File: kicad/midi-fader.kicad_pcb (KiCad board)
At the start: 2 copper layers, 73.7 x 78.7 mm, 163 parts, among them J1 SWD, J2 EXTERNAL_OUT, J3 EXTERNAL_IN, J4 USB_OTG, SW1 TR2-21-L5, SW2 TR2-21-L5, U1 STM32F042KxT, U2 USBLC6-2, U3 MCP1603, U4 MIC2776L, U5 MIC5501-XYM5, U6 74HC165, U7 STP08DP05

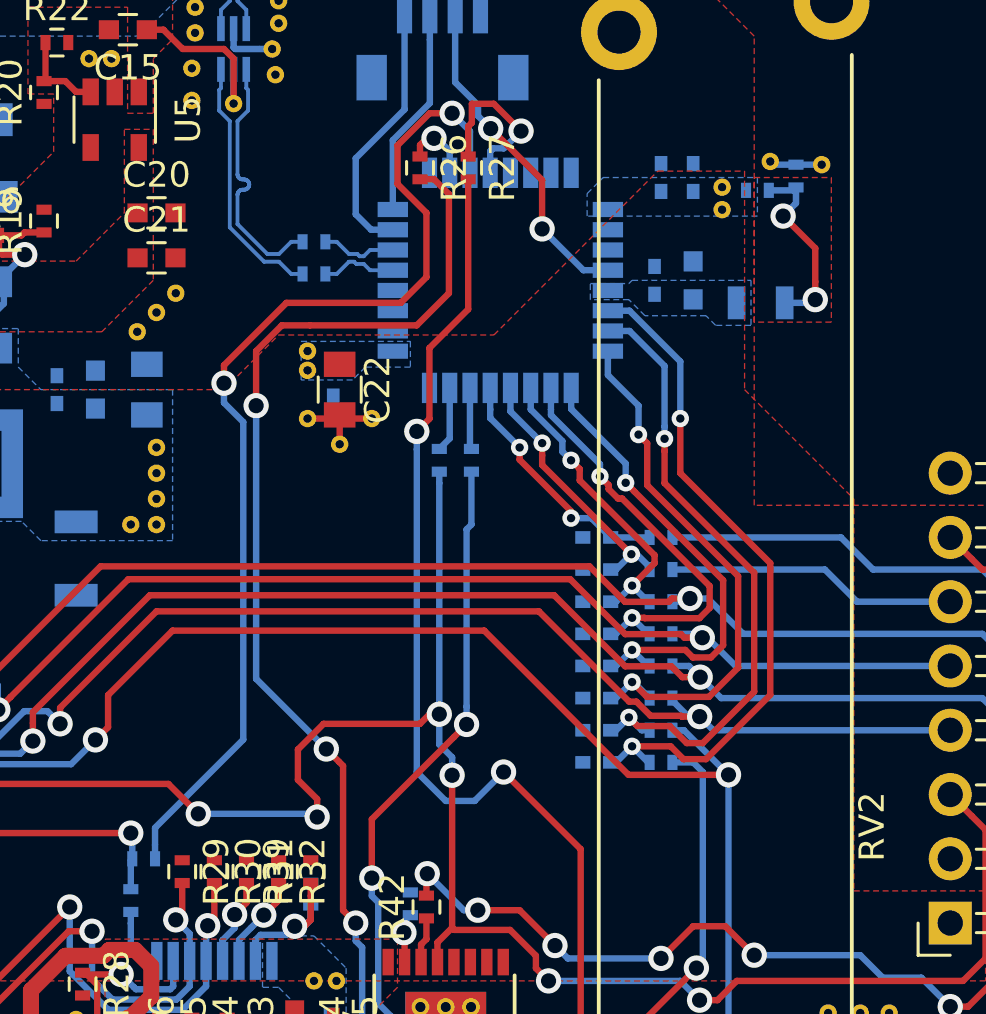
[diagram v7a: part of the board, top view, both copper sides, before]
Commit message: Marked no-connects and changed some plane shapes
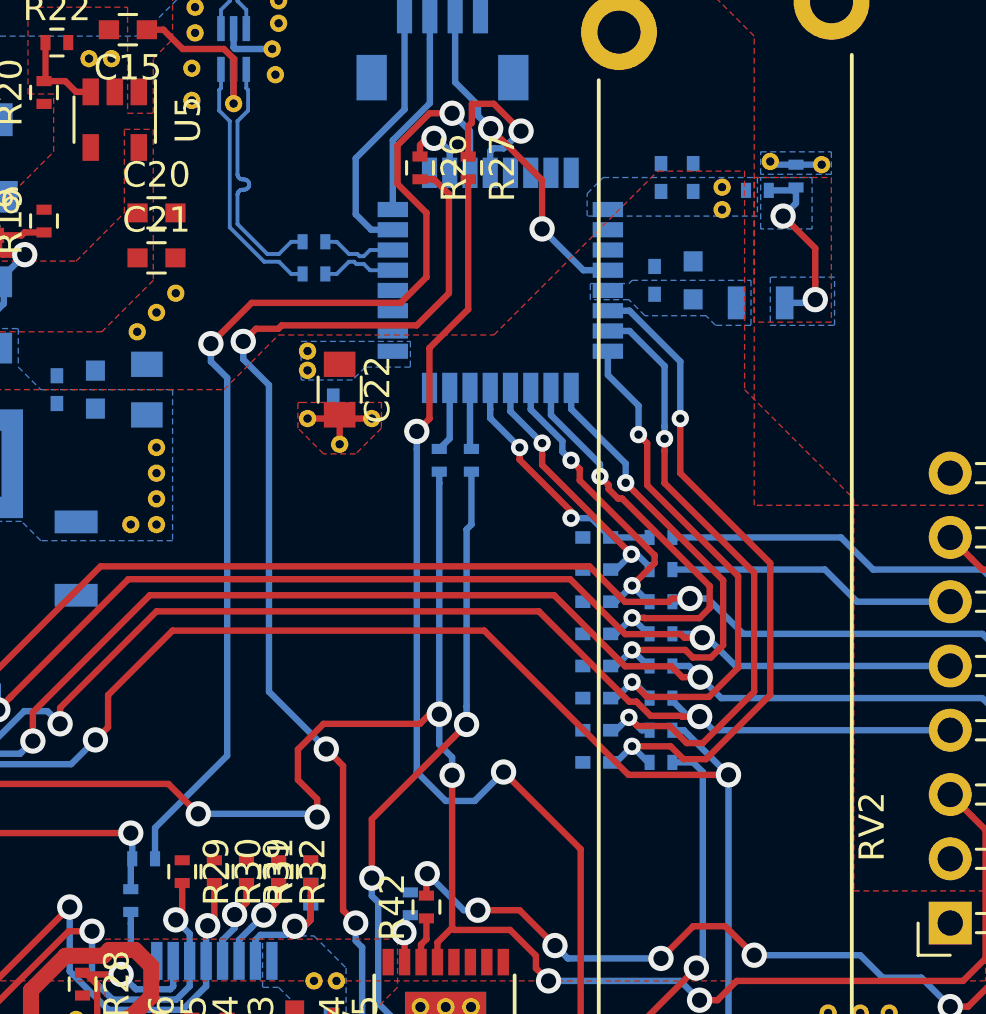
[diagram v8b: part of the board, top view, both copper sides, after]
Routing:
- net /Digital Control/SCLK: track 126.4 -> 127.3 mm
- net /Digital Control/MISO: track 41.7 -> 42.4 mm
- added copper zone on B.Cu, net /Digital Control/VDDA_UC_PREFILT
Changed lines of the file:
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@@
     (thickness 1.6)
     (drawings 9)
-    (tracks 961)
+    (tracks 960)
     (zones 0)
     (modules 163)
@@
     (pad_to_mask_clearance 0.1524)
     (aux_axis_origin 0 0)
+    (grid_origin 117.221 141.859)
     (visible_elements FFFFFF7F)
     (pcbplotparams
@@
   (segment (start 154.94 105.609106) (end 155.194 105.863106) (width 0.254) (layer B.Cu) (net 56))
   (via (at 154.94 104.902) (size 1) (drill 0.6) (layers F.Cu B.Cu) (net 56))
+  (segment (start 149.86 83.693) (end 150.359999 83.193001) (width 0.254) (layer F.Cu) (net 57))
+  (segment (start 157.988 81.788) (end 157.988 77.874) (width 0.254) (layer F.Cu) (net 57))
+  (segment (start 157.988 77.874) (end 157.399 77.285) (width 0.254) (layer F.Cu) (net 57))
+  (segment (start 150.359999 83.193001) (end 151.248999 83.193001) (width 0.254) (layer F.Cu) (net 57))
+  (segment (start 151.248999 83.193001) (end 151.384 83.058) (width 0.254) (layer F.Cu) (net 57))
+  (segment (start 151.384 83.058) (end 156.718 83.058) (width 0.254) (layer F.Cu) (net 57))
+  (segment (start 156.718 83.058) (end 157.988 81.788) (width 0.254) (layer F.Cu) (net 57))
+  (segment (start 157.399 77.285) (end 156.845 77.285) (width 0.254) (layer F.Cu) (net 57))
+  (segment (start 153.141627 99.801627) (end 150.876 97.536) (width 0.254) (layer B.Cu) (net 57))
+  (segment (start 150.876 97.536) (end 150.876 85.416106) (width 0.254) (layer B.Cu) (net 57))
+  (segment (start 150.876 85.416106) (end 149.86 84.400106) (width 0.254) (layer B.Cu) (net 57))
+  (segment (start 149.86 84.400106) (end 149.86 83.693) (width 0.254) (layer B.Cu) (net 57))
+  (via (at 149.86 83.693) (size 1) (drill 0.6) (layers F.Cu B.Cu) (net 57))
   (segment (start 177.673 114.427) (end 170.942 121.158) (width 0.254) (layer B.Cu) (net 57))
   (segment (start 170.942 121.158) (end 159.512 121.158) (width 0.254) (layer B.Cu) (net 57))
@@
   (via (at 156.972 116.713) (size 1) (drill 0.6) (layers F.Cu B.Cu) (net 57))
   (segment (start 156.886 113.773) (end 156.886 116.627) (width 0.254) (layer F.Cu) (net 57))
-  (segment (start 152.641628 99.301628) (end 153.141627 99.801627) (width 0.254) (layer B.Cu) (net 57))
-  (segment (start 150.368 97.028) (end 152.641628 99.301628) (width 0.254) (layer B.Cu) (net 57))
-  (segment (start 150.368 86.233) (end 150.368 97.028) (width 0.254) (layer B.Cu) (net 57))
   (segment (start 153.641626 100.301626) (end 153.141627 99.801627) (width 0.254) (layer F.Cu) (net 57))
   (segment (start 153.805001 100.465001) (end 153.641626 100.301626) (width 0.254) (layer F.Cu) (net 57))
@@
   (segment (start 154.305 107.387106) (end 154.559 107.641106) (width 0.254) (layer B.Cu) (net 57))
   (via (at 154.305 106.68) (size 1) (drill 0.6) (layers F.Cu B.Cu) (net 57))
-  (segment (start 151.384 83.058) (end 150.368 84.074) (width 0.254) (layer F.Cu) (net 57))
-  (segment (start 150.368 84.074) (end 150.368 86.233) (width 0.254) (layer F.Cu) (net 57))
-  (via (at 150.368 86.233) (size 1) (drill 0.6) (layers F.Cu B.Cu) (net 57))
-  (segment (start 152.494994 83.058) (end 151.384 83.058) (width 0.254) (layer F.Cu) (net 57))
-  (segment (start 156.718 83.058) (end 152.494994 83.058) (width 0.254) (layer F.Cu) (net 57))
-  (segment (start 157.988 81.788) (end 156.718 83.058) (width 0.254) (layer F.Cu) (net 57))
-  (segment (start 157.988 77.874) (end 157.988 81.788) (width 0.254) (layer F.Cu) (net 57))
-  (segment (start 156.845 77.285) (end 157.399 77.285) (width 0.254) (layer F.Cu) (net 57))
-  (segment (start 157.399 77.285) (end 157.988 77.874) (width 0.254) (layer F.Cu) (net 57))
   (segment (start 158.82 85.53) (end 158.82 87.885) (width 0.254) (layer B.Cu) (net 58))
   (segment (start 158.82 87.885) (end 158.877 87.942) (width 0.254) (layer B.Cu) (net 58))
@@
   (segment (start 145.288 112.903) (end 145.288 111.829) (width 0.254) (layer F.Cu) (net 70))
   (via (at 145.288 112.903) (size 1) (drill 0.6) (layers F.Cu B.Cu) (net 70))
-  (segment (start 146.373 103.586) (end 146.373 104.14) (width 0.254) (layer B.Cu) (net 71))
-  (segment (start 146.373 102.917486) (end 146.373 103.586) (width 0.254) (layer B.Cu) (net 71))
-  (segment (start 149.86 86.878514) (end 149.86 99.430486) (width 0.254) (layer B.Cu) (net 71))
-  (segment (start 149.098 85.344) (end 149.098 86.116514) (width 0.254) (layer B.Cu) (net 71))
-  (segment (start 149.86 99.430486) (end 146.373 102.917486) (width 0.254) (layer B.Cu) (net 71))
-  (segment (start 149.098 86.116514) (end 149.86 86.878514) (width 0.254) (layer B.Cu) (net 71))
-  (segment (start 149.098 84.636894) (end 149.098 85.344) (width 0.254) (layer F.Cu) (net 71))
-  (segment (start 156.083 82.169) (end 151.565894 82.169) (width 0.254) (layer F.Cu) (net 71))
-  (segment (start 157.099 81.153) (end 156.083 82.169) (width 0.254) (layer F.Cu) (net 71))
-  (segment (start 151.565894 82.169) (end 149.098 84.636894) (width 0.254) (layer F.Cu) (net 71))
-  (segment (start 157.099 78.613) (end 157.099 81.153) (width 0.254) (layer F.Cu) (net 71))
-  (segment (start 155.956 77.47) (end 157.099 78.613) (width 0.254) (layer F.Cu) (net 71))
-  (segment (start 155.956 75.946) (end 155.956 77.47) (width 0.254) (layer F.Cu) (net 71))
-  (segment (start 157.226 74.676) (end 155.956 75.946) (width 0.254) (layer F.Cu) (net 71))
   (segment (start 158.115 74.676) (end 157.226 74.676) (width 0.254) (layer F.Cu) (net 71))
-  (via (at 149.098 85.344) (size 1) (drill 0.6) (layers F.Cu B.Cu) (net 71))
+  (segment (start 157.226 74.676) (end 155.956 75.946) (width 0.254) (layer F.Cu) (net 71))
+  (segment (start 155.956 75.946) (end 155.956 77.47) (width 0.254) (layer F.Cu) (net 71))
+  (segment (start 155.956 77.47) (end 157.099 78.613) (width 0.254) (layer F.Cu) (net 71))
+  (segment (start 157.099 78.613) (end 157.099 81.153) (width 0.254) (layer F.Cu) (net 71))
+  (segment (start 157.099 81.153) (end 156.083 82.169) (width 0.254) (layer F.Cu) (net 71))
+  (segment (start 156.083 82.169) (end 150.193293 82.169) (width 0.254) (layer F.Cu) (net 71))
+  (segment (start 150.193293 82.169) (end 148.581247 83.781046) (width 0.254) (layer F.Cu) (net 71))
+  (segment (start 146.373 104.14) (end 146.373 102.917486) (width 0.254) (layer B.Cu) (net 71))
+  (segment (start 146.373 102.917486) (end 149.225 100.065486) (width 0.254) (layer B.Cu) (net 71))
+  (segment (start 149.225 100.065486) (end 149.225 85.131905) (width 0.254) (layer B.Cu) (net 71))
+  (segment (start 149.225 85.131905) (end 148.581247 84.488152) (width 0.254) (layer B.Cu) (net 71))
+  (segment (start 148.581247 84.488152) (end 148.581247 83.781046) (width 0.254) (layer B.Cu) (net 71))
+  (via (at 148.581247 83.781046) (size 1) (drill 0.6) (layers F.Cu B.Cu) (net 71))
   (segment (start 158.82 75.381) (end 158.115 74.676) (width 0.254) (layer B.Cu) (net 71))
   (via (at 158.115 74.676) (size 1) (drill 0.6) (layers F.Cu B.Cu) (net 71))
@@
       )
     )
+  )
+  (zone (net 48) (net_name "/Digital Control/VDDA_UC_PREFILT") (layer B.Cu) (hatch edge 0.508)
+    (priority 2)
+    (connect_pads yes (clearance 0.254))
+    (min_thickness 0.254)
+    (fill yes (arc_segments 16) (thermal_gap 0.508) (thermal_bridge_width 0.508))
+    (polygon
+      (pts
+        (xy 170.307 77.216) (xy 172.339 77.216) (xy 172.339 79.248) (xy 170.307 79.248)
+      )
+    )
+  )
+  (zone (net 12) (net_name VDDA) (layer B.Cu) (hatch edge 0.508)
+    (priority 1)
+    (connect_pads yes (clearance 0.254))
+    (min_thickness 0.254)
+    (fill yes (arc_segments 16) (thermal_gap 0.508) (thermal_bridge_width 0.508))
+    (polygon
+      (pts
+        (xy 170.307 76.2) (xy 173.101 76.2) (xy 173.101 77.089) (xy 170.307 77.089)
+      )
+    )
+  )
+  (zone (net 48) (net_name "/Digital Control/VDDA_UC_PREFILT") (layer B.Cu) (hatch edge 0.508)
+    (priority 2)
+    (connect_pads yes (clearance 0.254))
+    (min_thickness 0.254)
+    (fill yes (arc_segments 16) (thermal_gap 0.508) (thermal_bridge_width 0.508))
+    (polygon
+      (pts
+        (xy 170.688 81.153) (xy 170.688 83.058) (xy 173.228 83.058) (xy 173.228 81.153)
+      )
+    )
+  )
+  (zone (net 2) (net_name GND) (layer F.Cu) (hatch edge 0.508)
+    (priority 3)
+    (connect_pads yes (clearance 0.254))
+    (min_thickness 0.254)
+    (fill yes (arc_segments 16) (thermal_gap 0.508) (thermal_bridge_width 0.508))
+    (polygon
+      (pts
+        (xy 152.146 86.106) (xy 155.321 86.106) (xy 155.321 87.122) (xy 154.305 88.138) (xy 153.035 88.138)
+        (xy 152.019 87.122) (xy 152.019 86.106)
+      )
+    )
